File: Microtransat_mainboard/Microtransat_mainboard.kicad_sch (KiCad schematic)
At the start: 18 parts, among them J1 Conn_01x08, J10 Conn_01x04, J101 12V IN, J2 Conn_01x02, J4 Conn_01x04, J5 Conn_01x05, J9 Conn_01x04, SW1 SW_SPST, U1 GPS 746, U2 SD Card Module 254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

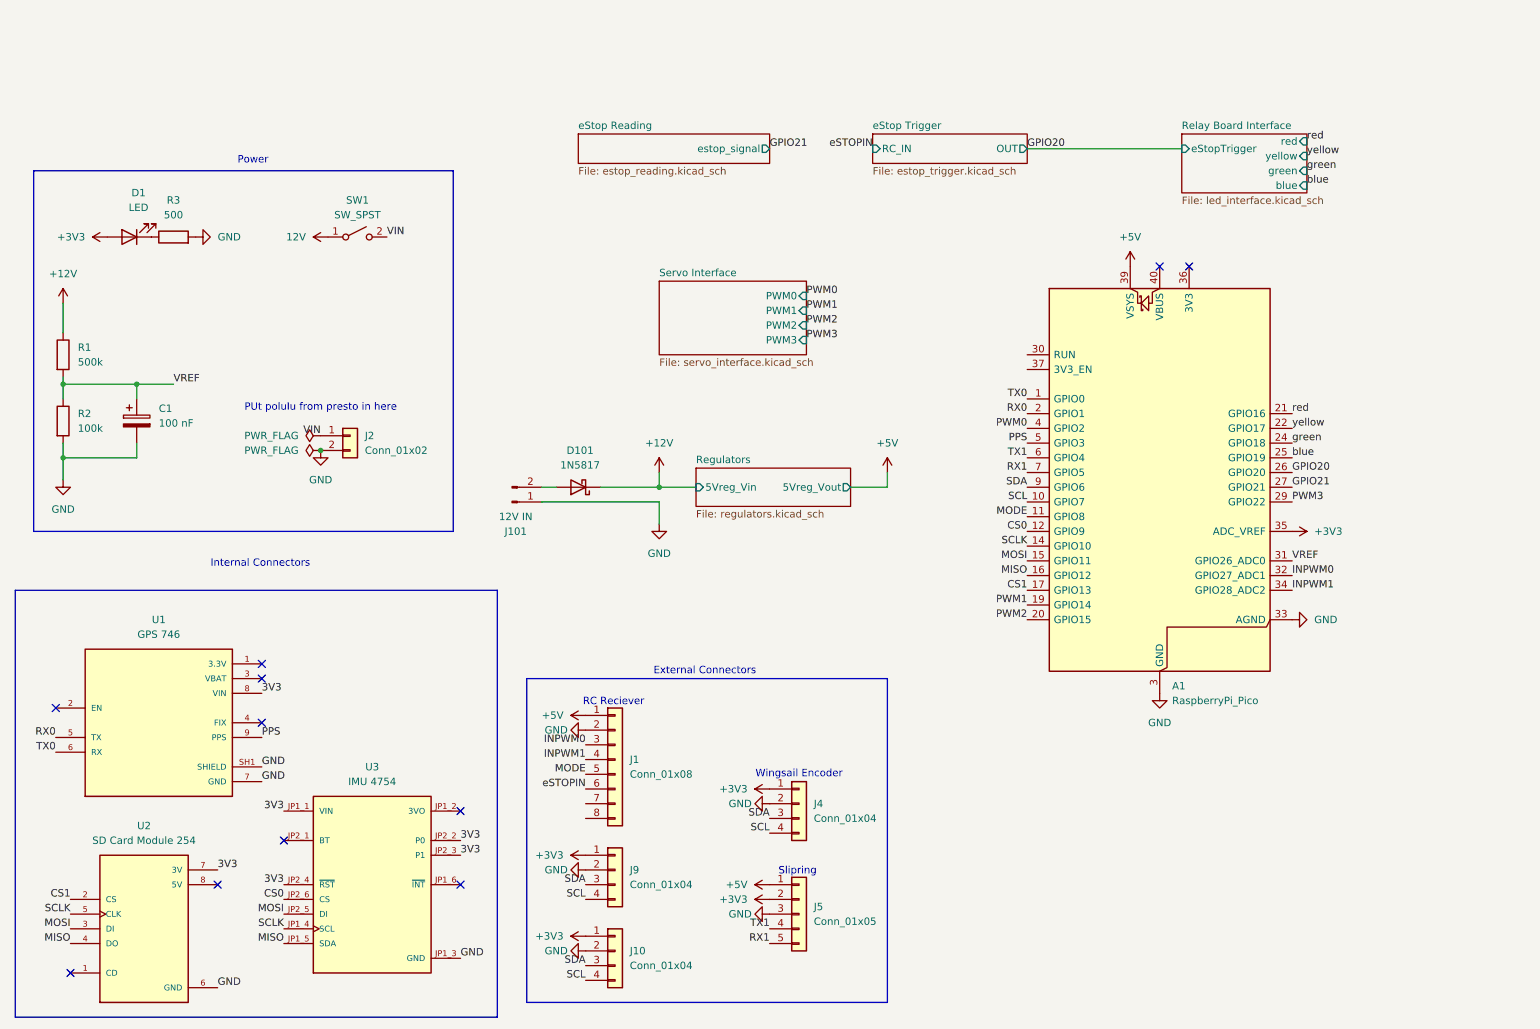
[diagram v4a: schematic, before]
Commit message: Fixed ERC errors
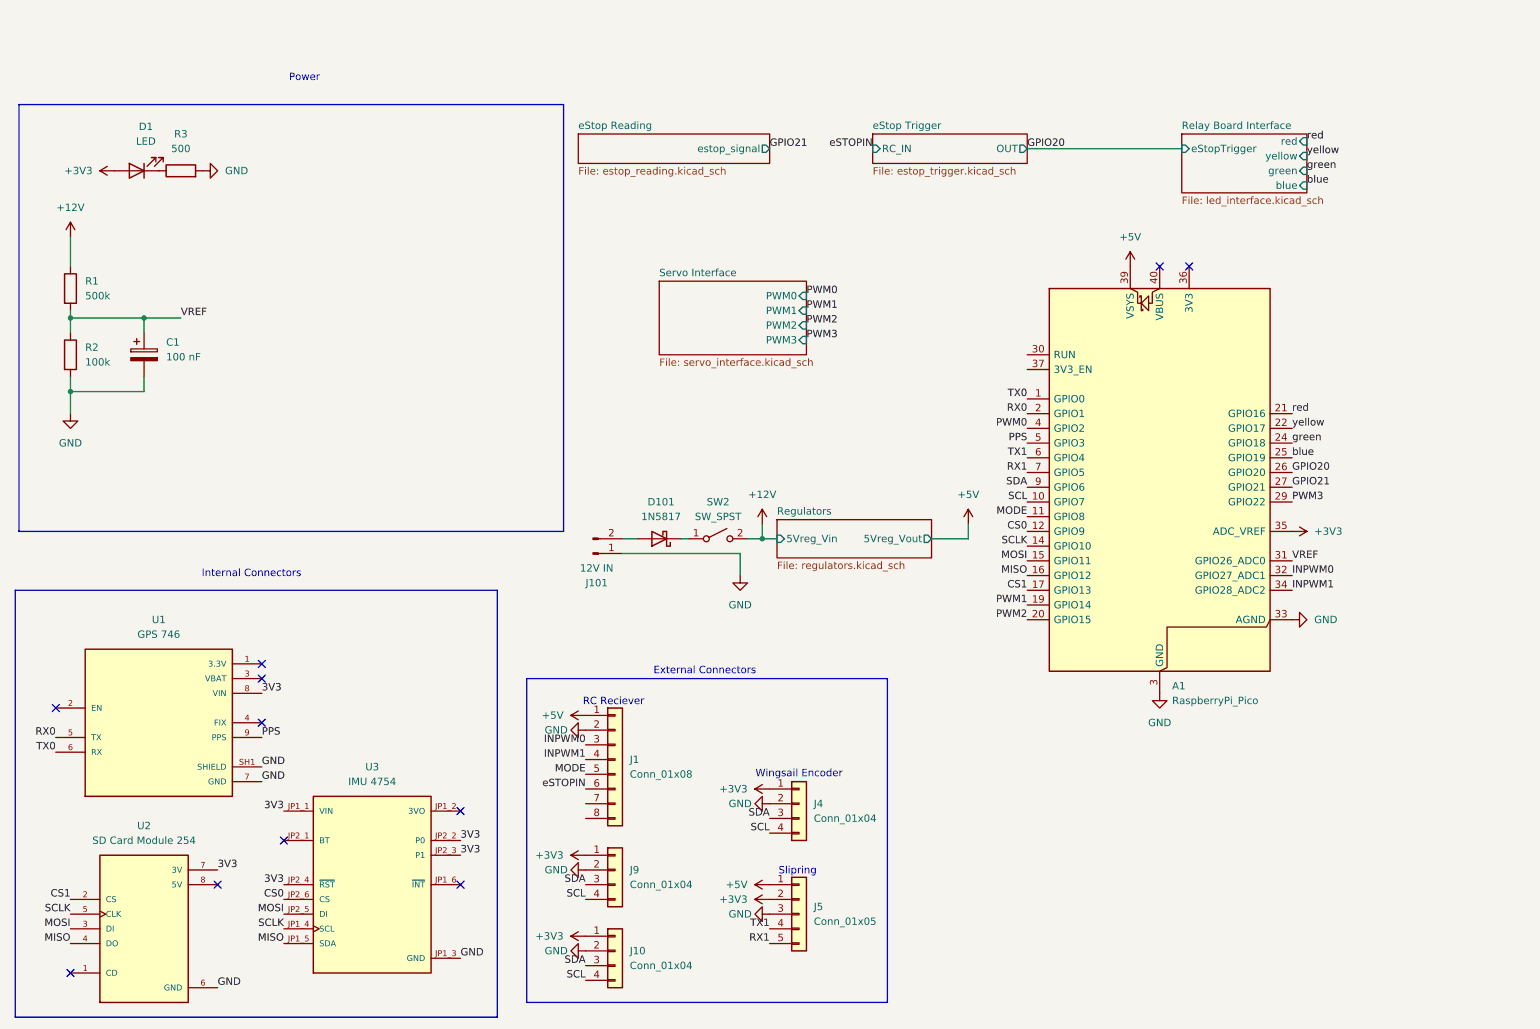
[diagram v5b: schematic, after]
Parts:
- removed J2: Conn_01x02, symbol Connector_Generic:Conn_01x02
- removed SW1: SW_SPST, symbol Switch:SW_SPST
- added SW2: SW_SPST, symbol Switch:SW_SPST
- C1: footprint (none) -> Capacitor_SMD:C_1206_3216Metric_Pad1.33x1.80mm_HandSolder
- D1: footprint (none) -> LED_SMD:LED_1206_3216Metric_Pad1.42x1.75mm_HandSolder
- J1: footprint (none) -> Connector_PinHeader_2.54mm:PinHeader_1x08_P2.54mm_Vertical
- J10, J9: footprint (none) -> Connector_JST:JST_XH_S4B-XH-A_1x04_P2.50mm_Horizontal
- J4: footprint (none) -> Connector_PinHeader_2.54mm:PinHeader_1x04_P2.54mm_Vertical
- J5: footprint (none) -> Connector_PinHeader_2.54mm:PinHeader_1x05_P2.54mm_Vertical
- R1, R2, R3: footprint (none) -> Resistor_SMD:R_1206_3216Metric_Pad1.30x1.75mm_HandSolder
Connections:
- net +12V: now also SW2.2 (B); no longer D101.1 (K)
- new net: D101.1 (K), SW2.1 (A)
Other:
- note removed: "PUt polulu from presto in here"
- moved on the sheet: C1, D1, D101, J101, R1, R2, R3

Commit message: Added switch
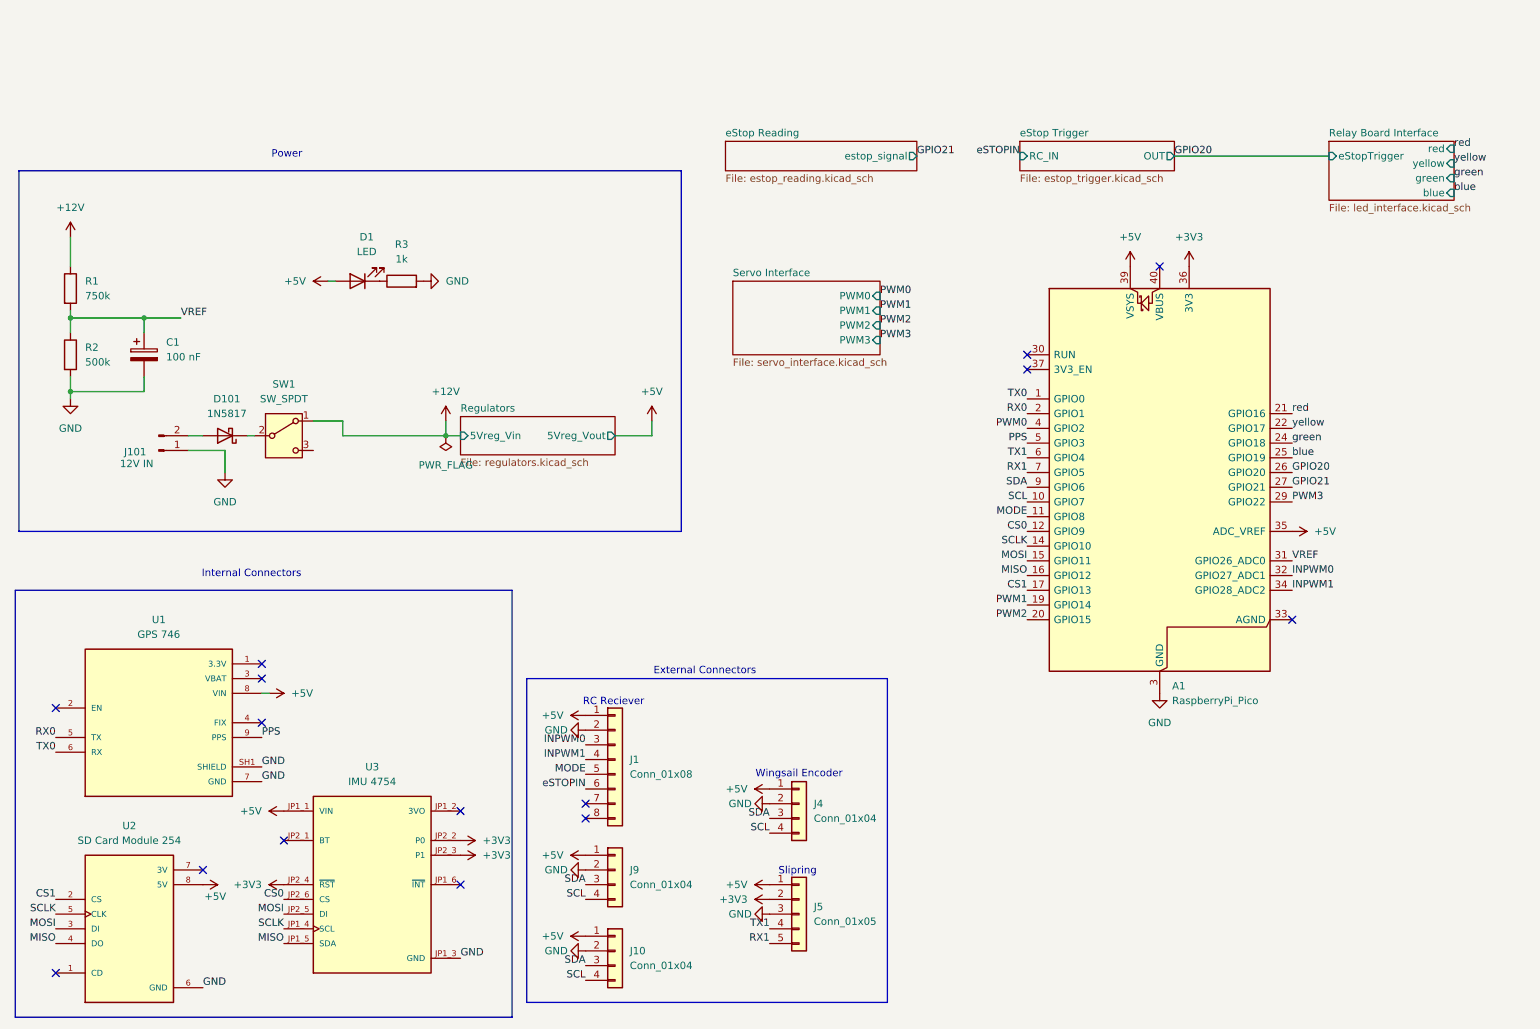
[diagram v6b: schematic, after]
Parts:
- removed SW2: SW_SPST, symbol Switch:SW_SPST
- added SW1: SW_SPDT, Microtransat:SW_EG1218, symbol Switch:SW_SPDT
- R1: value 500k -> 750k
- R2: value 100k -> 500k
- R3: value 500 -> 1k
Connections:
- net +12V: now also SW1.1 (A)
- net +3V3: now also A1.36 (3V3), U3.JP2_2 (P0), U3.JP2_3 (P1), U3.JP2_4 (~{RST}); no longer A1.35 (ADC_VREF), D1.2 (A), J10.1 (Pin_1), J4.1 (Pin_1), J9.1 (Pin_1)
- net +5V: now also A1.35 (ADC_VREF), D1.2 (A), J10.1 (Pin_1), J4.1 (Pin_1), J9.1 (Pin_1), U1.8 (VIN), U2.8 (5V), U3.JP1_1 (VIN)
- net GND: no longer A1.33 (AGND)
- net at D101.1 (K): now also SW1.2 (B)
- removed net 3V3: U1.8 (VIN), U2.7 (3V), U3.JP1_1 (VIN), U3.JP2_2 (P0), U3.JP2_3 (P1), U3.JP2_4 (~{RST})
- no-connect marks 11 -> 15
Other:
- moved on the sheet: D1, D101, J101, R3, U2

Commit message: Updated footprints
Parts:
- J10, J9: footprint Connector_JST:JST_XH_S4B-XH-A_1x04_P2.50mm_Horizontal -> Connector_JST:JST_XH_B4B-XH-A_1x04_P2.50mm_Vertical
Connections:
- no-connect marks 15 -> 16
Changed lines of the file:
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@@
 		(at 194.31 77.47)
 	)
+	(no_connect
+		(at 71.12 93.98)
+	)
 	(wire
 		(pts
@@
 			)
 		)
-		(property "Footprint" "Connector_JST:JST_XH_S4B-XH-A_1x04_P2.50mm_Horizontal"
+		(property "Footprint" "Connector_JST:JST_XH_B4B-XH-A_1x04_P2.50mm_Vertical"
 			(at 123.19 166.37 0)
 			(effects
@@
 			)
 		)
-		(property "Footprint" "Connector_JST:JST_XH_S4B-XH-A_1x04_P2.50mm_Horizontal"
+		(property "Footprint" "Connector_JST:JST_XH_B4B-XH-A_1x04_P2.50mm_Vertical"
 			(at 123.19 180.34 0)
 			(effects

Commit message: Started PCB
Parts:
- removed J5: Conn_01x05, Connector_PinHeader_2.54mm:PinHeader_1x05_P2.54mm_Vertical, symbol Connector_Generic:Conn_01x05
- added J2: Conn_01x04, Connector_JST:JST_XH_B4B-XH-A_1x04_P2.50mm_Vertical, symbol Connector_Generic:Conn_01x04
- J4: footprint Connector_PinHeader_2.54mm:PinHeader_1x04_P2.54mm_Vertical -> Connector_JST:JST_XH_B4B-XH-A_1x04_P2.50mm_Vertical
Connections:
- net +5V: now also J2.1 (Pin_1)
- net GND: now also J2.2 (Pin_2)
- net RX1: now also J2.4 (Pin_4)
- net TX1: now also J2.3 (Pin_3)
